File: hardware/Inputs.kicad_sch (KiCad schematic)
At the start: 52 parts, among them J13 Conn_01x05, J14 Conn_01x05, J15 Conn_01x05, J16 Conn_01x05, J17 Conn_01x05, J18 Conn_01x05, J19 Conn_01x03, J20 Conn_01x03, J21 Conn_01x03, J22 Conn_01x03, J23 Conn_01x03, J24 Conn_01x03, J25 Conn_01x02, J26 Conn_01x02, J27 FTSH-107-01-L-D-K

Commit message: Added Voltage reference, fixed silkscreen and BOM
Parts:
- J13, J14, J15, J16, J17, J18: Manufacturer_Part_Number (none) -> 2601-1105; Mouser (none) -> https://www.wago.com/pl/z%C5%82%C4%85czki-do-p%C5%82ytek-dr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; Mouser No (none) -> ---
- J19, J20, J21, J22, J23, J24: Manufacturer_Part_Number (none) -> 2601-1103; Mouser (none) -> https://www.wago.com/pl/z%C5%82%C4%85czki-do-p%C5%82ytek-dr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; Mouser No (none) -> ---
- J25, J26: Manufacturer_Part_Number (none) -> strain relief; Mouser (none) -> ---; Mouser No (none) -> ---
- J27: Manufacturer_Part_Nuber FTSH-107-01-L-D-K -> (none); Manufacturer_Part_Number (none) -> FTSH-107-01-L-D-K

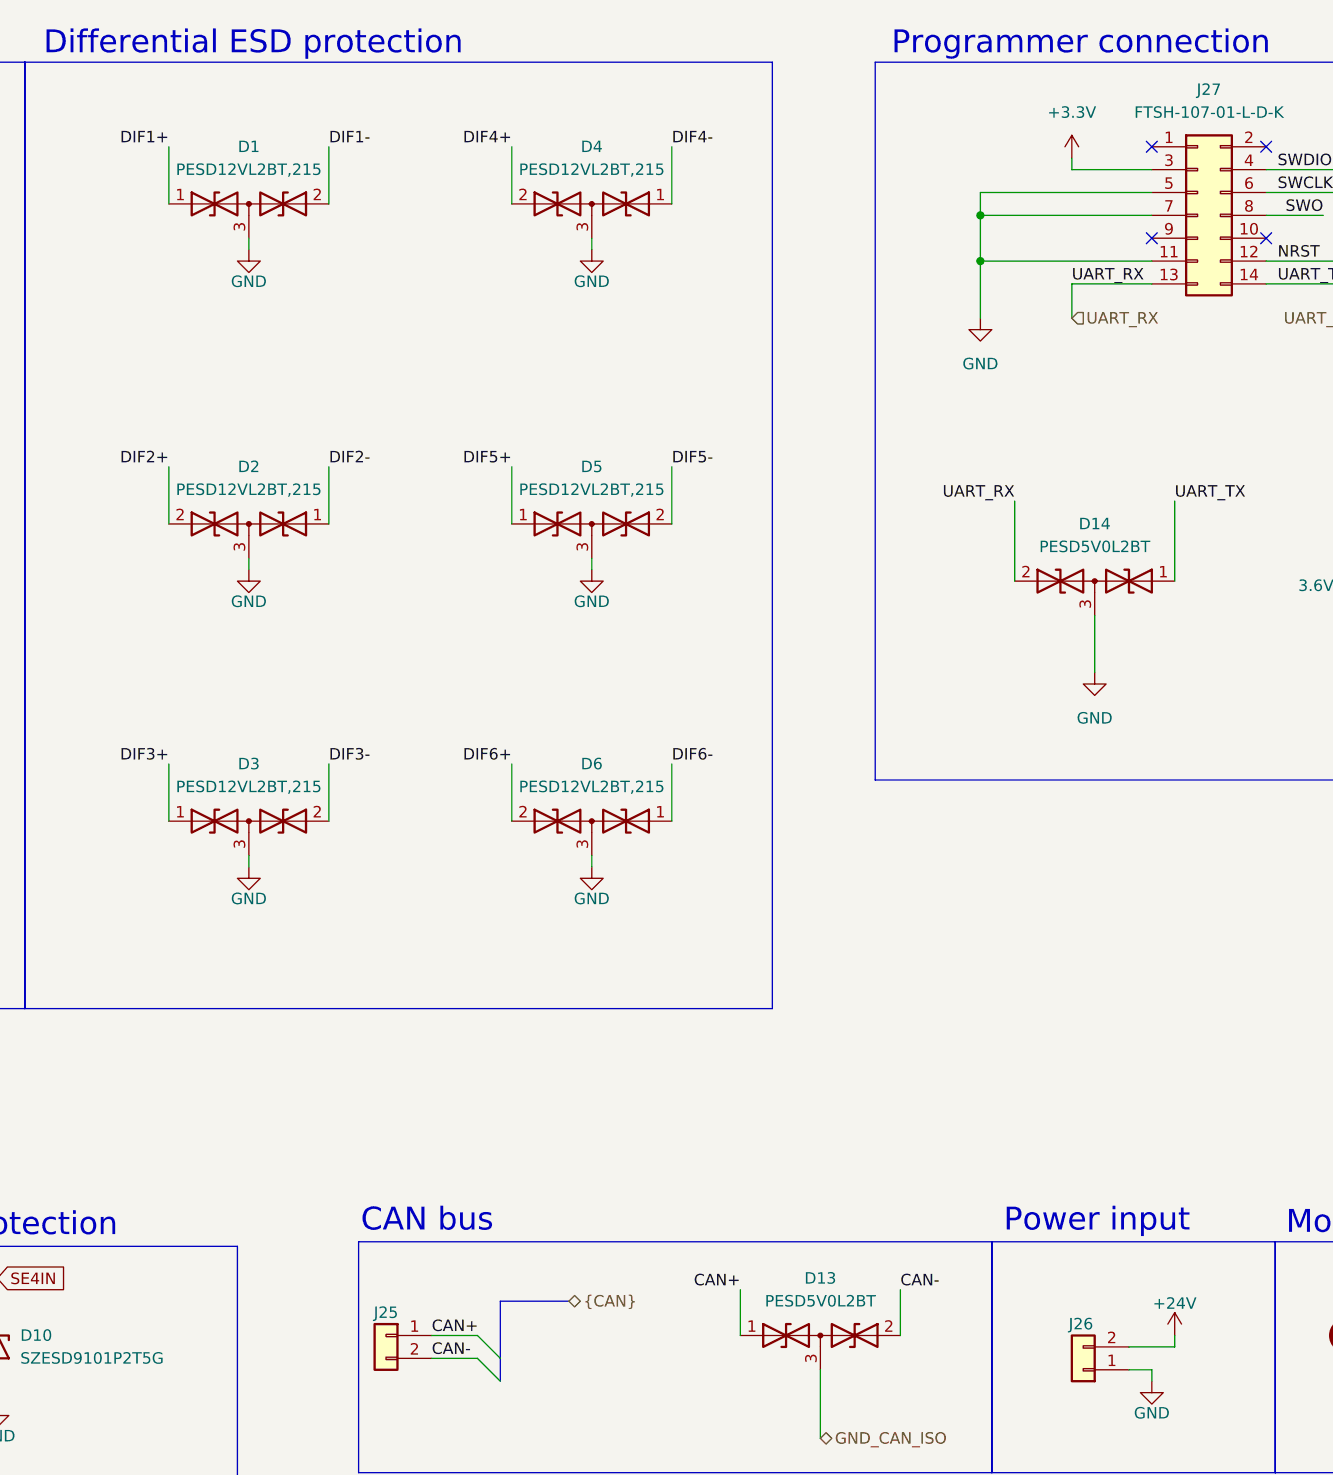
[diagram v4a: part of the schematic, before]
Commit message: Changed some components - they were non stocked
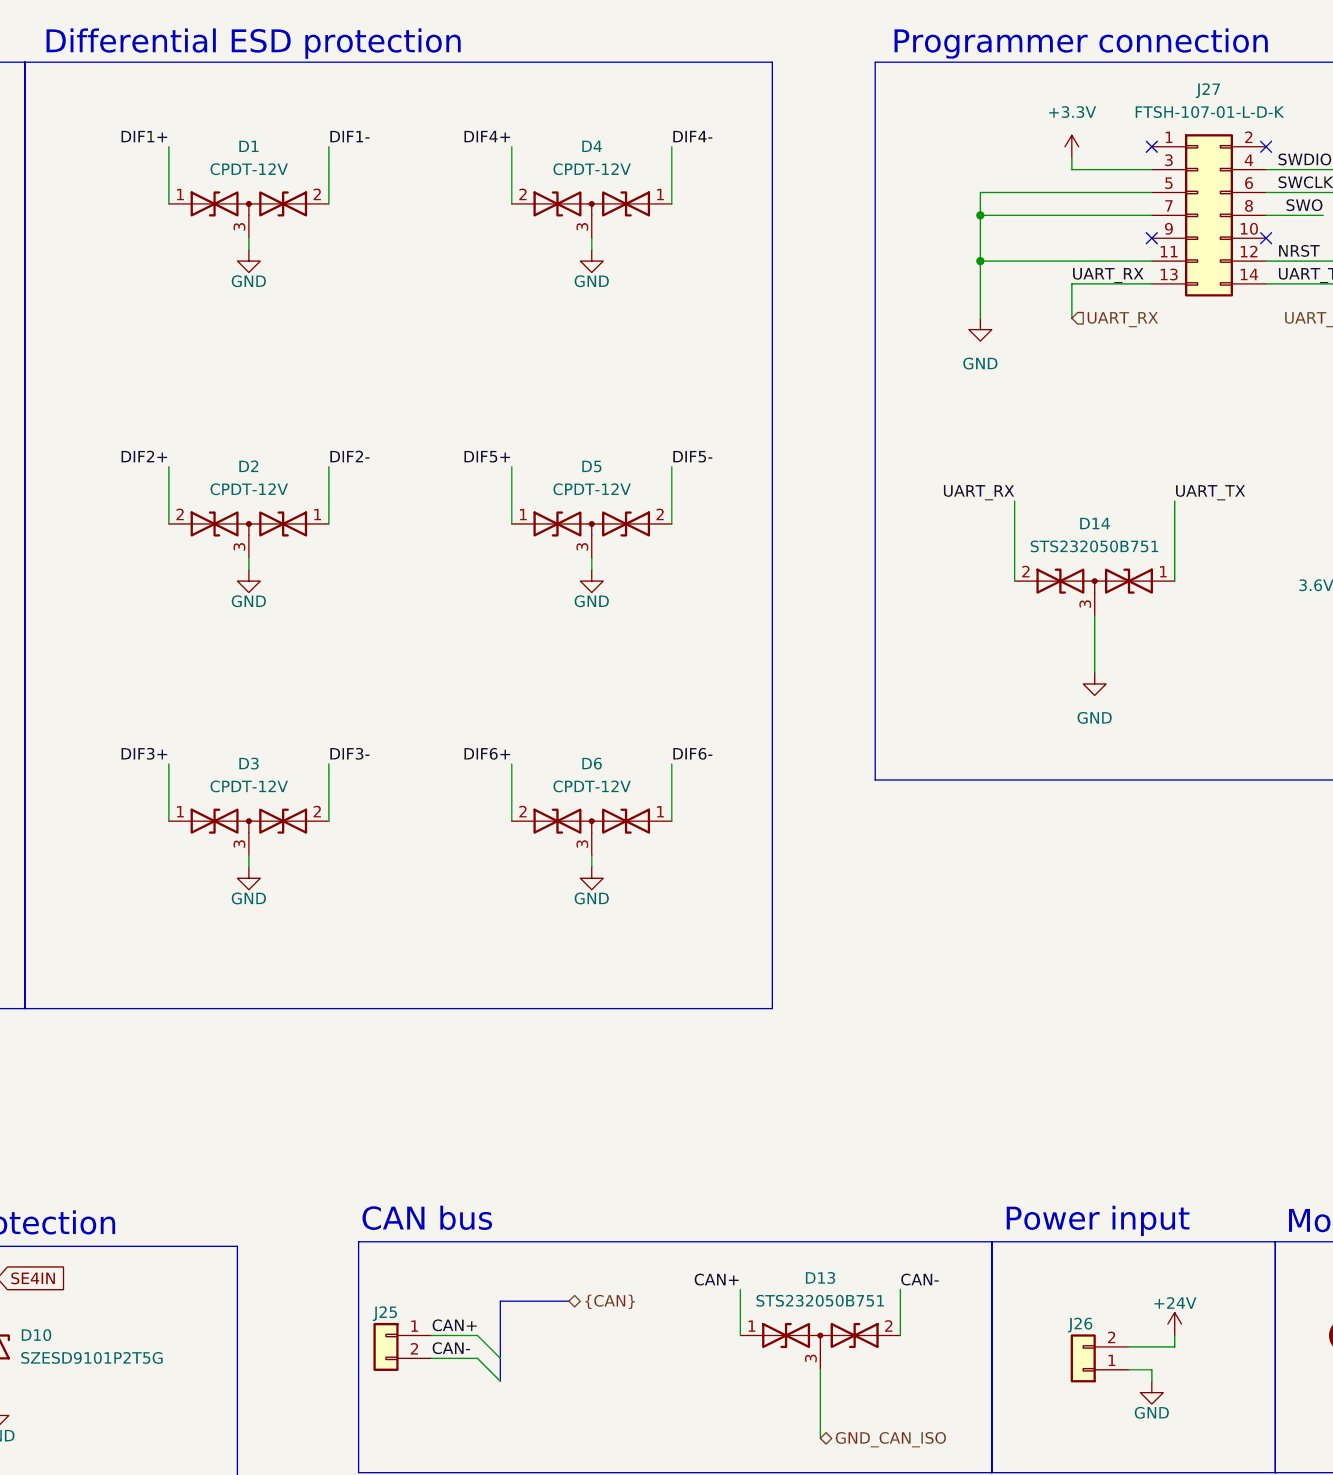
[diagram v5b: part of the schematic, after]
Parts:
- D1, D2, D3, D4, D5, D6: value PESD12VL2BT,215 -> CPDT-12V; Manufacturer_Part_Number D5V0L2B3W-7 -> CPDT-12V; Mouser https://www.mouser.pl/ProductDetail/Diodes-Incorporated/D5V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 -> https://www.mouser.pl/ProductDetail/Comchip-Technology/CPDT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; Mouser No 621-D5V0L2B3W-7 -> 750-CPDT-12V
- D10, D11, D12, D7, D8, D9: Manufacturer_Part_Number SZESD9101P2T5G -> SESD9L5.0ST5G; Mouser https://www.mouser.pl/ProductDetail/onsemi/SZESD9101P2T5G?q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 -> https://www.mouser.pl/ProductDetail/onsemi/SESD9L5.0ST5G?qs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; Mouser No 863-SZESD9101P2T5G -> 863-SESD9L5.0ST5G
- D13, D14: value PESD5V0L2BT -> STS232050B751; Manufacturer_Part_Number PESD5V0L2BT-QR -> STS232050B751; Mouser https://www.mouser.pl/ProductDetail/Nexperia/PESD5V0L2BT-QR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 -> https://www.mouser.pl/ProductDetail/Eaton-Electronics/STS23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; Mouser No 771-PESD5V0L2BT-QR -> 504-STS232050B751

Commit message: hardware sync
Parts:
- D10, D11, D12, D7, D8, D9: value SZESD9101P2T5G -> CDSOD323-T05S; footprint Diode_SMD:D_SOD-923 -> 5VtvsUnidir:SOD2513X114N; Manufacturer_Part_Number SESD9L5.0ST5G -> CDSOD323-T05S; Mouser https://www.mouser.pl/ProductDetail/onsemi/SESD9L5.0ST5G?qs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 -> https://www.mouser.pl/ProductDetail/Bourns/CDSOD323-T05S?qs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; Mouser No 863-SESD9L5.0ST5G -> 652-CDSOD323-T05S
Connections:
- net UART_RX: now also J27.14 (Pin_14); no longer J27.13 (Pin_13)
- net UART_TX: now also J27.13 (Pin_13); no longer J27.14 (Pin_14)
